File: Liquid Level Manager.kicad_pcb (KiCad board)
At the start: 2 copper layers, 89.2 x 82 mm, 19 parts, among them J1 Valve, J3 +12V, Q1 IRLB8721PBF, U1 High Sensor, U2 Low Sensor, U3 74LS02, U4 LM7805C

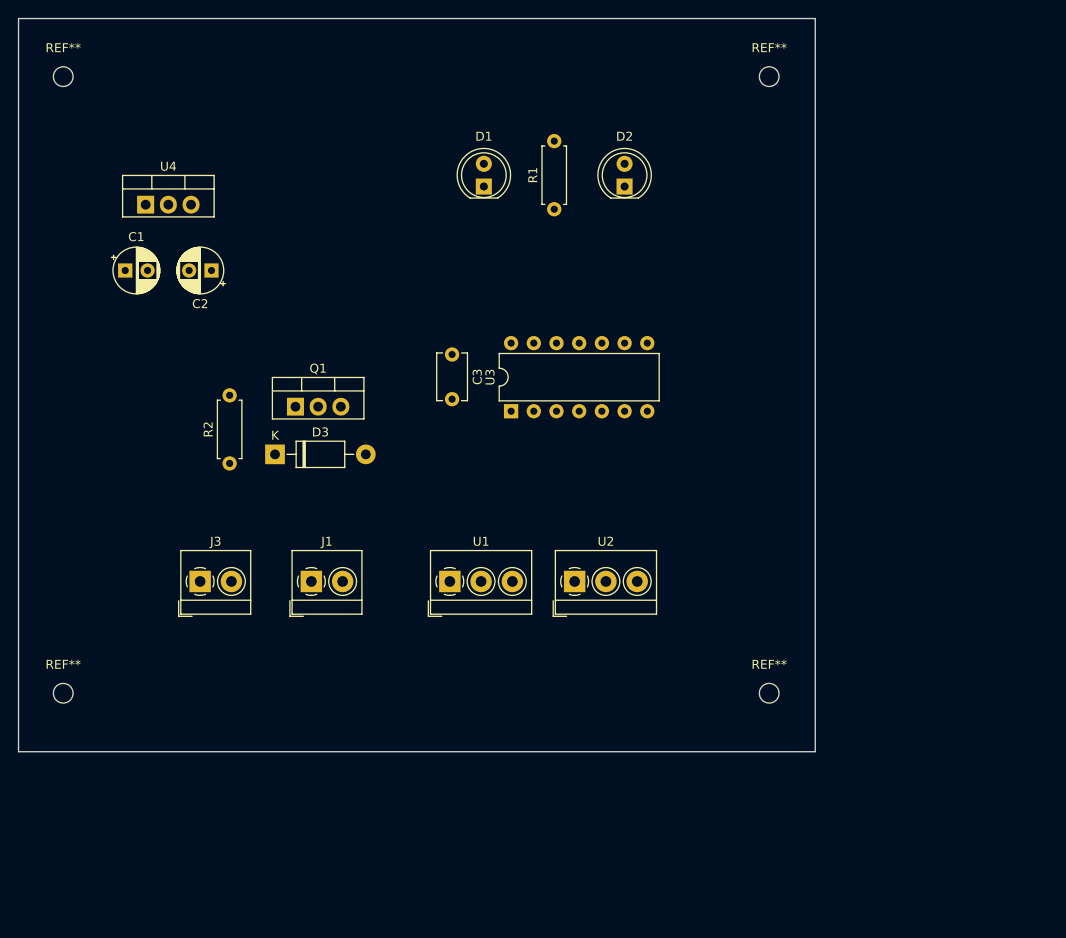
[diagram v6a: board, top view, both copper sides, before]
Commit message: updated design rules
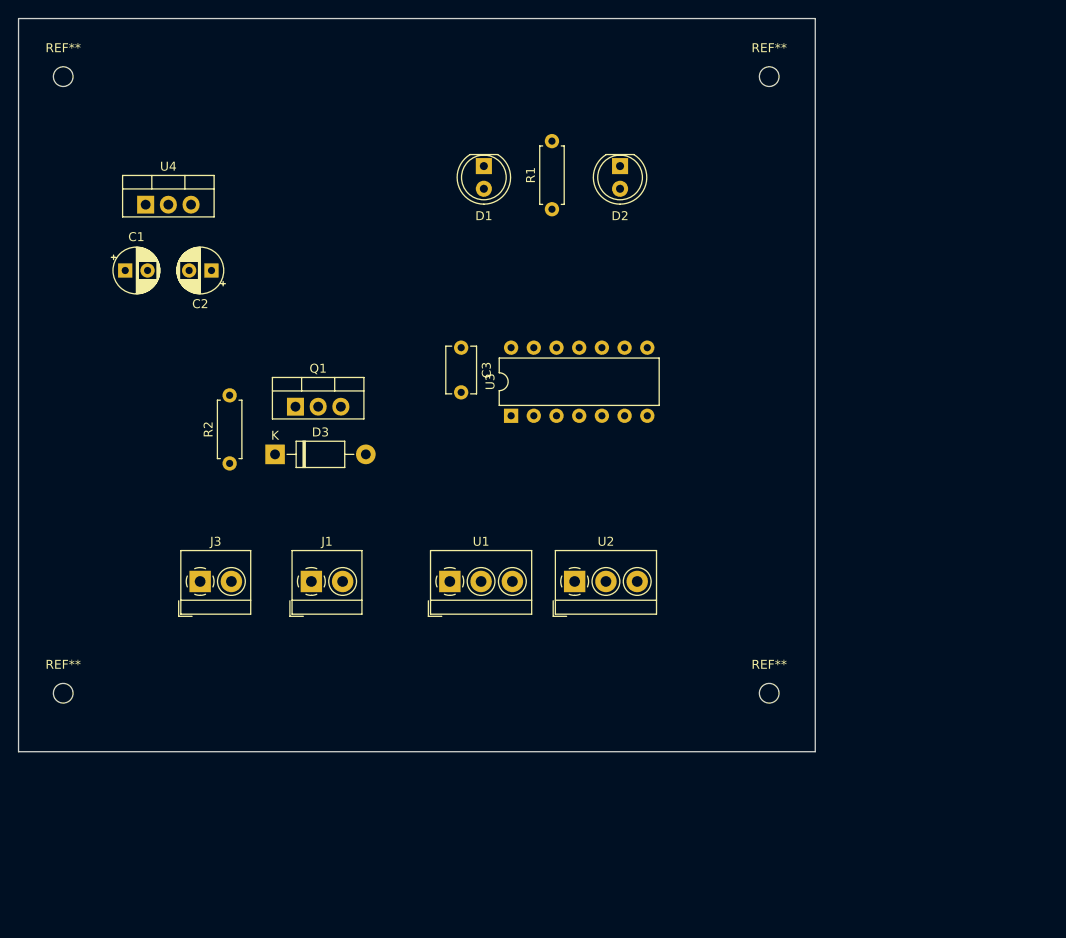
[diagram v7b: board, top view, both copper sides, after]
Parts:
- moved D2 2.34 mm to (164.3, 59.7), turned to 270 degrees
- moved D1 2.29 mm to (149.1, 59.7), turned to 270 degrees
- moved C3 1.27 mm to (146.6, 80.0)
- moved U3 0.51 mm to (152.1, 87.6)
- moved R1 0.25 mm to (156.7, 64.5)
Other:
- net class Default: clearance 0.2 -> 0.254; trace_width 0.25 -> 0.254; via_dia 0.8 -> 0.762; via_drill 0.4 -> 0.381
- rule pad_to_mask_clearance: 0.051 -> 0.002
- rule trace_clearance: 0.2 -> 0.254
- rule trace_min: 0.2 -> 0.1524
- rule via_min_drill: 0.3 -> 0.3302
- rule via_min_size: 0.4 -> 0.6858
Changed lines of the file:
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@@
   )
   (setup
-    (last_trace_width 0.25)
-    (trace_clearance 0.2)
+    (last_trace_width 0.254)
+    (trace_clearance 0.254)
     (zone_clearance 0.508)
     (zone_45_only no)
-    (trace_min 0.2)
+    (trace_min 0.1524)
     (segment_width 0.2)
     (edge_width 0.15)
-    (via_size 0.8)
-    (via_drill 0.4)
-    (via_min_size 0.4)
-    (via_min_drill 0.3)
-    (uvia_size 0.3)
-    (uvia_drill 0.1)
+    (via_size 0.762)
+    (via_drill 0.381)
+    (via_min_size 0.6858)
+    (via_min_drill 0.3302)
+    (uvia_size 0.762)
+    (uvia_drill 0.381)
     (uvias_allowed no)
-    (uvia_min_size 0.2)
-    (uvia_min_drill 0.1)
+    (uvia_min_size 0.6858)
+    (uvia_min_drill 0.3302)
     (pcb_text_width 0.3)
     (pcb_text_size 1.5 1.5)
@@
     (pad_size 1.524 1.524)
     (pad_drill 0.762)
-    (pad_to_mask_clearance 0.051)
-    (solder_mask_min_width 0.25)
+    (pad_to_mask_clearance 0.002)
     (aux_axis_origin 0 0)
     (grid_origin 97.028 43.18)
@@
   (net 11 SENSOR_OUT)
   (net_class Default "This is the default net class."
-    (clearance 0.2)
-    (trace_width 0.25)
-    (via_dia 0.8)
-    (via_drill 0.4)
-    (uvia_dia 0.3)
-    (uvia_drill 0.1)
+    (clearance 0.254)
+    (trace_width 0.254)
+    (via_dia 0.762)
+    (via_drill 0.381)
+    (uvia_dia 0.762)
+    (uvia_drill 0.381)
+    (diff_pair_gap 0.254)
+    (diff_pair_width 0.254)
     (add_net +12V)
     (add_net +5V)
@@
   )
   (module LED_THT:LED_D5.0mm (layer F.Cu)
-    (at 149.098 61.976 90)
+    (at 149.098 59.69 270)
     (descr "LED, diameter 5.0mm, 2 pins, http://cdn-reichelt.de/documents/datenblatt/A500/LL-504BC2E-009.pdf")
     (tags "LED diameter 5.0mm 2 pins")
-    (fp_text reference D1 (at 5.588 0 180) (layer F.SilkS)
-      (effects (font (size 1 1) (thickness 0.15)))
-    )
-    (fp_text value Good (at -3.048 0 180) (layer F.Fab)
-      (effects (font (size 1 1) (thickness 0.15)))
-    )
-    (fp_text user %R (at 1.25 0 90) (layer F.Fab)
+    (fp_text reference D1 (at 5.588 0) (layer F.SilkS)
+      (effects (font (size 1 1) (thickness 0.15)))
+    )
+    (fp_text value Good (at -3.048 0) (layer F.Fab)
+      (effects (font (size 1 1) (thickness 0.15)))
+    )
+    (fp_text user %R (at 1.25 0 270) (layer F.Fab)
       (effects (font (size 0.8 0.8) (thickness 0.2)))
     )
@@
     (fp_arc (start 1.27 0) (end -1.29 -1.54483) (angle 148.9) (layer F.SilkS) (width 0.12))
     (fp_arc (start 1.27 0) (end -1.23 -1.469694) (angle 299.1) (layer F.Fab) (width 0.1))
-    (pad 2 thru_hole circle (at 2.54 0 90) (size 1.8 1.8) (drill 0.9) (layers *.Cu *.Mask)
+    (pad 2 thru_hole circle (at 2.54 0 270) (size 1.8 1.8) (drill 0.9) (layers *.Cu *.Mask)
       (net 1 "Net-(D1-Pad2)"))
-    (pad 1 thru_hole rect (at 0 0 90) (size 1.8 1.8) (drill 0.9) (layers *.Cu *.Mask)
+    (pad 1 thru_hole rect (at 0 0 270) (size 1.8 1.8) (drill 0.9) (layers *.Cu *.Mask)
       (net 8 "Net-(D1-Pad1)"))
     (model ${KISYS3DMOD}/LED_THT.3dshapes/LED_D5.0mm.wrl
@@
   )
   (module LED_THT:LED_D5.0mm (layer F.Cu)
-    (at 164.846 61.976 90)
+    (at 164.338 59.69 270)
     (descr "LED, diameter 5.0mm, 2 pins, http://cdn-reichelt.de/documents/datenblatt/A500/LL-504BC2E-009.pdf")
     (tags "LED diameter 5.0mm 2 pins")
-    (fp_text reference D2 (at 5.588 0 180) (layer F.SilkS)
-      (effects (font (size 1 1) (thickness 0.15)))
-    )
-    (fp_text value Filling (at -3.048 0 180) (layer F.Fab)
+    (fp_text reference D2 (at 5.588 0) (layer F.SilkS)
+      (effects (font (size 1 1) (thickness 0.15)))
+    )
+    (fp_text value Filling (at -3.048 0) (layer F.Fab)
       (effects (font (size 1 1) (thickness 0.15)))
     )
@@
     (fp_line (start 4.5 3.25) (end 4.5 -3.25) (layer F.CrtYd) (width 0.05))
     (fp_line (start 4.5 -3.25) (end -1.95 -3.25) (layer F.CrtYd) (width 0.05))
-    (fp_text user %R (at 1.25 0 90) (layer F.Fab)
+    (fp_text user %R (at 1.25 0 270) (layer F.Fab)
       (effects (font (size 0.8 0.8) (thickness 0.2)))
     )
-    (pad 1 thru_hole rect (at 0 0 90) (size 1.8 1.8) (drill 0.9) (layers *.Cu *.Mask)
+    (pad 1 thru_hole rect (at 0 0 270) (size 1.8 1.8) (drill 0.9) (layers *.Cu *.Mask)
       (net 8 "Net-(D1-Pad1)"))
-    (pad 2 thru_hole circle (at 2.54 0 90) (size 1.8 1.8) (drill 0.9) (layers *.Cu *.Mask)
+    (pad 2 thru_hole circle (at 2.54 0 270) (size 1.8 1.8) (drill 0.9) (layers *.Cu *.Mask)
       (net 11 SENSOR_OUT))
     (model ${KISYS3DMOD}/LED_THT.3dshapes/LED_D5.0mm.wrl
@@
   )
   (module Package_DIP:DIP-14_W7.62mm (layer F.Cu)
-    (at 152.146 87.122 90)
+    (at 152.146 87.63 90)
     (descr "14-lead though-hole mounted DIP package, row spacing 7.62 mm (300 mils)")
     (tags "THT DIP DIL PDIP 2.54mm 7.62mm 300mil")
@@
   )
   (module Capacitor_THT:C_Disc_D5.1mm_W3.2mm_P5.00mm (layer F.Cu)
-    (at 145.542 80.772 270)
+    (at 146.558 80.01 270)
     (descr "C, Disc series, Radial, pin pitch=5.00mm, , diameter*width=5.1*3.2mm^2, Capacitor, http://www.vishay.com/docs/45233/krseries.pdf")
     (tags "C Disc series Radial pin pitch 5.00mm  diameter 5.1mm width 3.2mm Capacitor")
@@
   )
   (module Resistor_THT:R_Axial_DIN0207_L6.3mm_D2.5mm_P7.62mm_Horizontal (layer F.Cu)
-    (at 156.972 64.516 90)
+    (at 156.718 64.516 90)
     (descr "Resistor, Axial_DIN0207 series, Axial, Horizontal, pin pitch=7.62mm, 0.25W = 1/4W, length*diameter=6.3*2.5mm^2, http://cdn-reichelt.de/documents/datenblatt/B400/1_4W%23YAG.pdf")
     (tags "Resistor Axial_DIN0207 series Axial Horizontal pin pitch 7.62mm 0.25W = 1/4W length 6.3mm diameter 2.5mm")
@@
     )
   )
-  (module TerminalBlock_4Ucon:TerminalBlock_4Ucon_1x02_P3.50mm_Horizontal (layer F.Cu)
+  (module TerminalBlock_4Ucon:TerminalBlock_4Ucon_1x02_P3.50mm_Horizontal locked (layer F.Cu)
     (at 129.794 106.172)
     (descr "Terminal Block 4Ucon ItemNo. 19963, 2 pins, pitch 3.5mm, size 7.7x7mm^2, drill diamater 1.2mm, pad diameter 2.4mm, see http://www.4uconnector.com/online/object/4udrawing/19963.pdf, script-generated using https://github.com/pointhi/kicad-footprint-generator/scripts/TerminalBlock_4Ucon")
@@
     )
   )
-  (module TerminalBlock_4Ucon:TerminalBlock_4Ucon_1x03_P3.50mm_Horizontal (layer F.Cu)
+  (module TerminalBlock_4Ucon:TerminalBlock_4Ucon_1x03_P3.50mm_Horizontal locked (layer F.Cu)
     (at 145.288 106.172)
     (descr "Terminal Block 4Ucon ItemNo. 20193, 3 pins, pitch 3.5mm, size 11.2x7mm^2, drill diamater 1.2mm, pad diameter 2.4mm, see http://www.4uconnector.com/online/object/4udrawing/20193.pdf, script-generated using https://github.com/pointhi/kicad-footprint-generator/scripts/TerminalBlock_4Ucon")
@@
     )
   )
-  (module TerminalBlock_4Ucon:TerminalBlock_4Ucon_1x03_P3.50mm_Horizontal (layer F.Cu)
+  (module TerminalBlock_4Ucon:TerminalBlock_4Ucon_1x03_P3.50mm_Horizontal locked (layer F.Cu)
     (at 159.258 106.172)
     (descr "Terminal Block 4Ucon ItemNo. 20193, 3 pins, pitch 3.5mm, size 11.2x7mm^2, drill diamater 1.2mm, pad diameter 2.4mm, see http://www.4uconnector.com/online/object/4udrawing/20193.pdf, script-generated using https://github.com/pointhi/kicad-footprint-generator/scripts/TerminalBlock_4Ucon")
@@
     )
   )
-  (module TerminalBlock_4Ucon:TerminalBlock_4Ucon_1x02_P3.50mm_Horizontal (layer F.Cu)
+  (module TerminalBlock_4Ucon:TerminalBlock_4Ucon_1x02_P3.50mm_Horizontal locked (layer F.Cu)
     (at 117.348 106.172)
     (descr "Terminal Block 4Ucon ItemNo. 19963, 2 pins, pitch 3.5mm, size 7.7x7mm^2, drill diamater 1.2mm, pad diameter 2.4mm, see http://www.4uconnector.com/online/object/4udrawing/19963.pdf, script-generated using https://github.com/pointhi/kicad-footprint-generator/scripts/TerminalBlock_4Ucon")
@@
     )
   )
-  (gr_line (start 186.182 125.222) (end 97.028 125.222) (layer Edge.Cuts) (width 0.15))
-  (gr_line (start 186.182 43.18) (end 186.182 125.222) (layer Edge.Cuts) (width 0.15))
-  (gr_line (start 97.028 43.18) (end 186.182 43.18) (layer Edge.Cuts) (width 0.15))
-  (gr_line (start 97.028 125.222) (end 97.028 43.18) (layer Edge.Cuts) (width 0.15))
+  (gr_line (start 186.182 125.222) (end 97.028 125.222) (layer Edge.Cuts) (width 0.0254))
+  (gr_line (start 186.182 43.18) (end 186.182 125.222) (layer Edge.Cuts) (width 0.0254))
+  (gr_line (start 97.028 43.18) (end 186.182 43.18) (layer Edge.Cuts) (width 0.0254))
+  (gr_line (start 97.028 125.222) (end 97.028 43.18) (layer Edge.Cuts) (width 0.0254))
 )

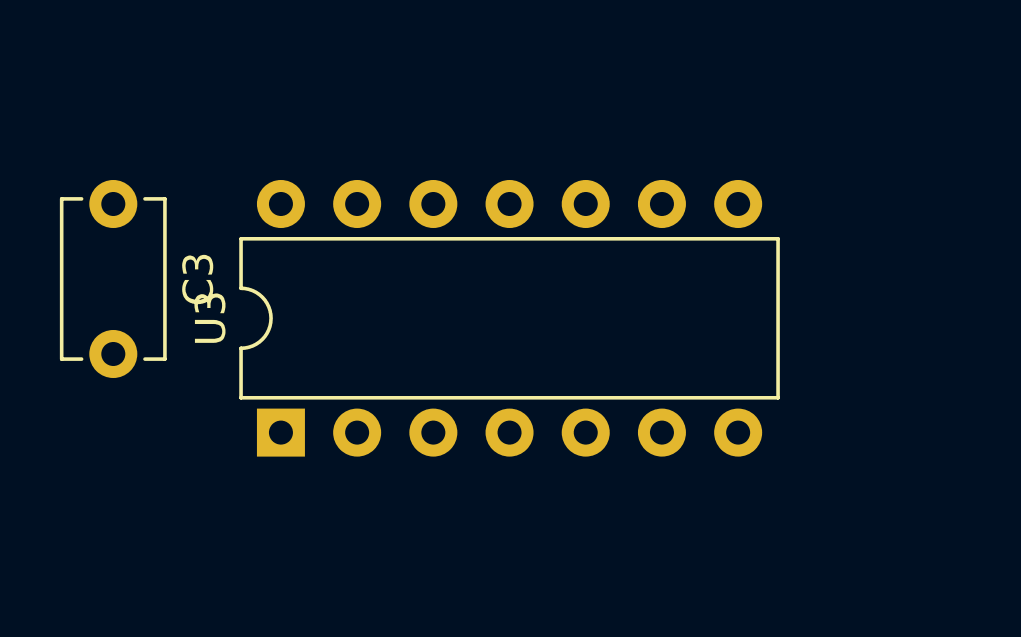
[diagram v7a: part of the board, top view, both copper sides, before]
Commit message: added custom trace width for high-current power
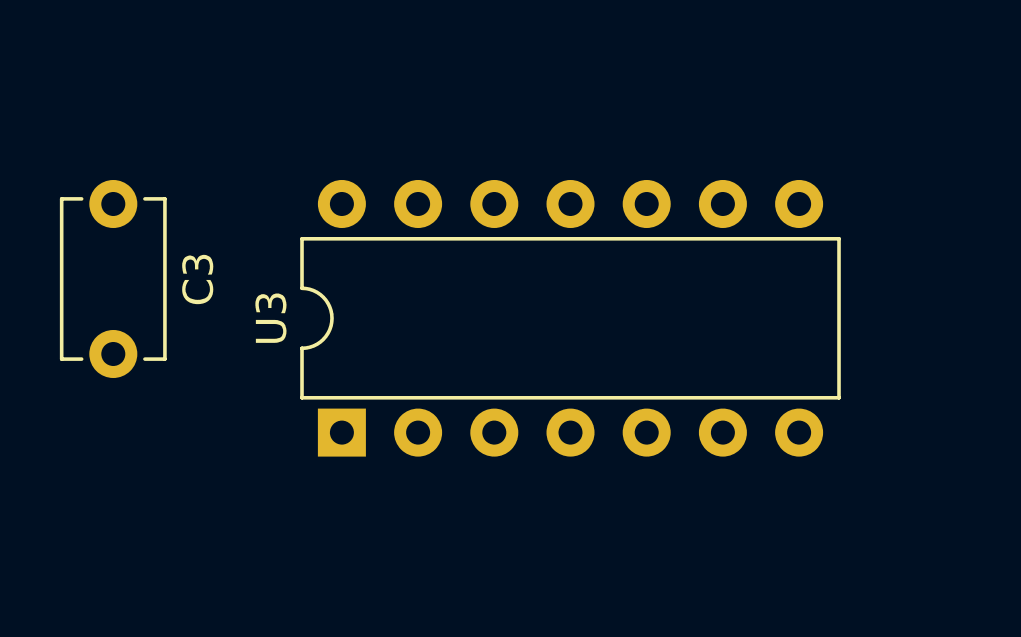
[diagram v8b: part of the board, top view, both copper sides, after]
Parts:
- moved U3 2.03 mm to (154.2, 87.6)
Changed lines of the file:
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@@
   (setup
     (last_trace_width 0.254)
+    (user_trace_width 2.032863)
     (trace_clearance 0.254)
     (zone_clearance 0.508)
@@
   )
   (module Package_DIP:DIP-14_W7.62mm (layer F.Cu)
-    (at 152.146 87.63 90)
+    (at 154.178 87.63 90)
     (descr "14-lead though-hole mounted DIP package, row spacing 7.62 mm (300 mils)")
     (tags "THT DIP DIL PDIP 2.54mm 7.62mm 300mil")
